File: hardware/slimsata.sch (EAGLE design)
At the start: 2 parts, among them CON1 MOLEX_67492, CON2 MOLEX_47300

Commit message: Package des Molex 447300 von -1005 zu 1020 geändert
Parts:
- CON2: device sata:MOLEX_47300100X/101X -> sata:MOLEX_47300102X/103X
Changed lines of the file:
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@@
 <parts>
 <part name="CON1" library="sata" deviceset="MOLEX_67492" device=""/>
-<part name="CON2" library="sata" deviceset="MOLEX_47300" device="100X/101X" value="MOLEX_47300"/>
+<part name="CON2" library="sata" deviceset="MOLEX_47300" device="102X/103X" value="MOLEX_47300"/>
 </parts>
 <sheets>

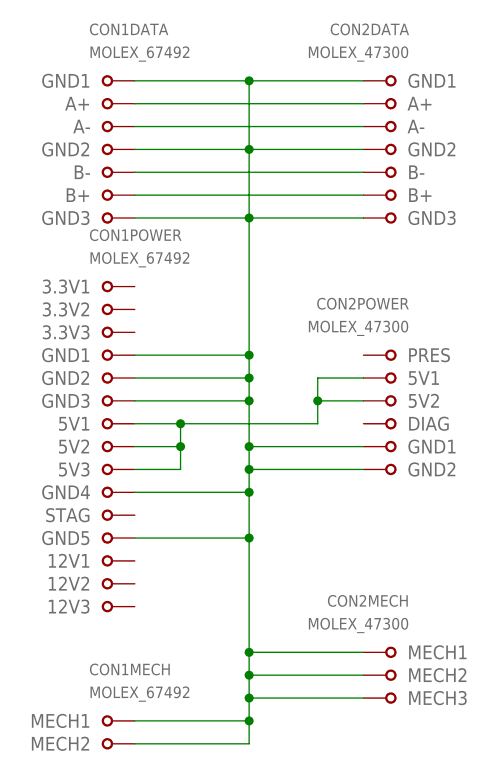
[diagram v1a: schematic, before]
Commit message: Molex 47300 durch Kombivariante ersetzt
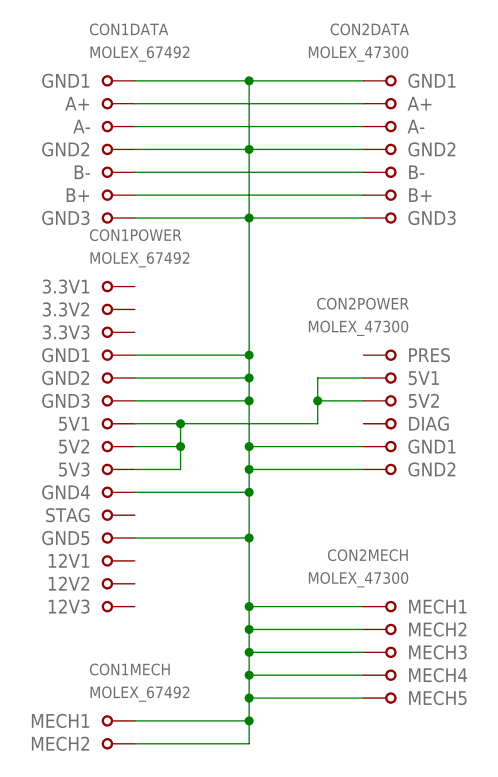
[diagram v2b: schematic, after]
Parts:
- CON2: device sata:MOLEX_47300102X/103X -> sata:MOLEX_47300_KOMBI
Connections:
- net GND: now also CON2MECH.MECH4, CON2MECH.MECH5
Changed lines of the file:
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@@
 <parts>
 <part name="CON1" library="sata" deviceset="MOLEX_67492" device=""/>
-<part name="CON2" library="sata" deviceset="MOLEX_47300" device="102X/103X" value="MOLEX_47300"/>
+<part name="CON2" library="sata" deviceset="MOLEX_47300_KOMBI" device="" value="MOLEX_47300"/>
 </parts>
 <sheets>
@@
 <instance part="CON2" gate="DATA" x="43.18" y="73.66" rot="MR0"/>
 <instance part="CON2" gate="POWER" x="43.18" y="43.18" rot="MR0"/>
-<instance part="CON2" gate="MECH" x="43.18" y="15.24" rot="MR0"/>
+<instance part="CON2" gate="MECH" x="43.18" y="17.78" rot="MR0"/>
 </instances>
 <busses>
@@
 <segment>
 <pinref part="CON1" gate="MECH" pin="MECH2"/>
+<wire x1="30.48" y1="20.32" x2="30.48" y2="17.78" width="0.1524" layer="91"/>
 <wire x1="30.48" y1="17.78" x2="30.48" y2="15.24" width="0.1524" layer="91"/>
 <wire x1="30.48" y1="15.24" x2="30.48" y2="12.7" width="0.1524" layer="91"/>
@@
 <wire x1="17.78" y1="10.16" x2="30.48" y2="10.16" width="0.1524" layer="91"/>
 <junction x="30.48" y="10.16"/>
-<pinref part="CON2" gate="MECH" pin="MECH3"/>
-<wire x1="43.18" y1="12.7" x2="30.48" y2="12.7" width="0.1524" layer="91"/>
-<junction x="30.48" y="12.7"/>
-<pinref part="CON2" gate="MECH" pin="MECH2"/>
+<pinref part="CON2" gate="MECH" pin="MECH4"/>
 <wire x1="43.18" y1="15.24" x2="30.48" y2="15.24" width="0.1524" layer="91"/>
 <junction x="30.48" y="15.24"/>
-<pinref part="CON2" gate="MECH" pin="MECH1"/>
+<pinref part="CON2" gate="MECH" pin="MECH3"/>
 <wire x1="43.18" y1="17.78" x2="30.48" y2="17.78" width="0.1524" layer="91"/>
+<junction x="30.48" y="17.78"/>
+<pinref part="CON2" gate="MECH" pin="MECH2"/>
+<wire x1="43.18" y1="20.32" x2="30.48" y2="20.32" width="0.1524" layer="91"/>
 <pinref part="CON1" gate="POWER" pin="GND1"/>
 <wire x1="17.78" y1="50.8" x2="30.48" y2="50.8" width="0.1524" layer="91"/>
 <wire x1="30.48" y1="50.8" x2="30.48" y2="48.26" width="0.1524" layer="91"/>
-<junction x="30.48" y="17.78"/>
+<junction x="30.48" y="20.32"/>
 <pinref part="CON1" gate="POWER" pin="GND2"/>
 <wire x1="30.48" y1="48.26" x2="30.48" y2="45.72" width="0.1524" layer="91"/>
@@
 <wire x1="30.48" y1="38.1" x2="30.48" y2="35.56" width="0.1524" layer="91"/>
 <wire x1="30.48" y1="35.56" x2="30.48" y2="30.48" width="0.1524" layer="91"/>
-<wire x1="30.48" y1="30.48" x2="30.48" y2="17.78" width="0.1524" layer="91"/>
+<wire x1="30.48" y1="30.48" x2="30.48" y2="22.86" width="0.1524" layer="91"/>
+<wire x1="30.48" y1="22.86" x2="30.48" y2="20.32" width="0.1524" layer="91"/>
 <wire x1="17.78" y1="48.26" x2="30.48" y2="48.26" width="0.1524" layer="91"/>
 <junction x="30.48" y="48.26"/>
@@
 <wire x1="30.48" y1="66.04" x2="30.48" y2="50.8" width="0.1524" layer="91"/>
 <junction x="30.48" y="50.8"/>
+<pinref part="CON2" gate="MECH" pin="MECH1"/>
+<wire x1="43.18" y1="22.86" x2="30.48" y2="22.86" width="0.1524" layer="91"/>
+<junction x="30.48" y="22.86"/>
+<pinref part="CON2" gate="MECH" pin="MECH5"/>
+<wire x1="43.18" y1="12.7" x2="30.48" y2="12.7" width="0.1524" layer="91"/>
+<junction x="30.48" y="12.7"/>
 </segment>
 </net>
